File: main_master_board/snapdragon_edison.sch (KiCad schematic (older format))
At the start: 4 parts, among them U17 conn_2x45, U18 conn_2x45

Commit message: Added a lot of things. Put a 5v to 4v buck as well as supporing the snapdragon board
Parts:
- removed J?: USB_MICRO_RIGHT, MF_Connectors_MICROUSB-RIGHT, symbol USB_MICRO_RIGHT
- removed SD?: SD_CARD_SLOT_MICRO_RIGHT, MF_Connectors_MF-MICROSD, symbol SD_CARD_SLOT_MICRO_RIGHT
- added C33: 4.7uF, Capacitors_SMD:C_0603, symbol C_Small
- added C34, C35, C36, C37, C38, C39, C41, C42, C43, C44, C45, C46, C47, C48, C49, C50: 0.1uF, Capacitors_SMD:C_0402, symbol C_Small
- added C40: 1.0uF, Capacitors_SMD:C_0402, symbol C_Small
- added C53: 1.0uF, Capacitors_SMD:C_0603, symbol C_Small
- added C56, C57: 1uF, Capacitors_SMD:C_0603, symbol C_Small
- added J2: J0C-0005NLT, Pulse_Electronics:J0C, symbol RJ45
- added L4, L5: 2.0A/0.05 DCR, dp_devices2:dp_devices-C603, symbol Ferrite_Bead_Small
- added R24: 33, Resistors_SMD:R_0402, symbol R
- added R26: 825, Resistors_SMD:R_0603, symbol R
- added R27, R29: 10.0K, Resistors_SMD:R_0603, symbol R
- added R30: 12.4K, Resistors_SMD:R_0603, symbol R
- added R32: 12.0K, Resistors_SMD:R_0603, symbol R
- added R46, R47, R48, R50: 49.9, Resistors_SMD:R_0402, symbol R
- added R49: 10.0, Resistors_SMD:R_0402, symbol R
- added R56, R57, R58, R59: 33, Resistors_SMD:R_0402, symbol R_Small
- added R67, R68: 1K, Resistors_SMD:R_0402, symbol R
- added U19: LAN9512, Housings_DFN_QFN:QFN-64-1EP_9x9mm_Pitch0.5mm, symbol LAN9512
- added U21: MIC2026, SOIC_8:SOIC-8_N, symbol MIC2026
- added U24: AS1360, TO_SOT_Packages_SMD:SOT-23, symbol AS1360
- added U25: Si1900DL, NASA_IRG_SSB:SOT323-6, symbol Si1900DL
- added U26, U27: SN74LV4T125, VQFN-14:VQFN-14, symbol SN74LV4T125
- added U28: SN74LV1T125, TO_SOT_Packages_SMD:SC-70, symbol SN74LV1T125
- added Y1: SG-310SCCN 25.000MJ3, Seiko_Epson_Crystals:SG-310, symbol Crystal_GND24
- U17: value conn_2x45 -> J1; footprint Variscite:DART-SD410 -> MODULE
- U18: value conn_2x45 -> J2
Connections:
- net labels added: +1V8, +3.3VA, 1V8, APQ_RESIN_N, BBCLK2, BOOT_CONFIG_0, BOOT_CONFIG_1, BOOT_CONFIG_2, BOOT_CONFIG_3, BOOT_CONFIG_5, EEPROM_WP, FORCED_USB_BOOT, GPIO_105, GPIO_106, GPIO_107, GPIO_108, GPIO_109, GPIO_110, GPIO_112, GPIO_113, GPIO_114, GPIO_115, GPIO_116, GPIO_117, GPIO_118, GPIO_119, GPIO_12, GPIO_120, GPIO_13, GPIO_20, GPIO_21, GPIO_24, GPIO_25, GPIO_26, GPIO_27, GPIO_28, GPIO_29, GPIO_30, GPIO_31, GPIO_32, GPIO_33, GPIO_34, GPIO_35, GPIO_36, GPIO_49, GPIO_50, GPIO_51, GPIO_52, GPIO_62, GPIO_69, GPIO_96, GPIO_97, GPIO_98, I2C0_SCL, I2C0_SCL_3V3, I2C0_SDA, I2C0_SDA_3V3, I2C1_SCL, I2C1_SDA, I2C3_SCL, I2C3_SDA, JTAG_PS_HOLD, JTAG_SRST_N, JTAG_TCK, JTAG_TDI, JTAG_TDO, JTAG_TMS, JTAG_TRST_N, PM_GPIO1, PM_GPIO2, PM_GPIO3, PM_GPIO4, PM_MPP2, PM_MPP3, PM_MPP4, PM_RESIN_N, PRTCTL2, PRTCTL3, PWR2, PWR3, RXN, RXP, SDC2_CLK, SDC2_CMD, SDC2_DATA_0, SDC2_DATA_1, SDC2_DATA_2, SDC2_DATA_3, SD_CARD_DET_N, SPI0_CLK, SPI0_CS_N, SPI0_MISO, SPI0_MOSI, SPI1_CLK, SPI1_CLK_3V3, SPI1_CS_N, SPI1_CS_N_3V3, SPI1_MISO, SPI1_MISO_3V3, SPI1_MOSI, SPI1_MOSI_3V3, TXN, TXP, UART0_CTS_N, UART0_RTS_N, UART0_RX, UART0_TX, UART1_RX, UART1_RX_3V3, UART1_TX, UART1_TX_3V3, USBDM0, USBDM2, USBDP0, USBDP2, USBDP3, USBPM3, USB_HS_D_M, USB_HS_D_P, USB_HS_ID, USB_VBUS, VBUS_DET, VDD18ETHPLL, VDD18USBPLL, VREG_L11_SDC, VREG_L12_SDC, XI, nRESET, power_on/off, sensor_I2C_SCL, sensor_I2C_SDA, uC_CLK, uC_CS, uC_GPIO1, uC_GPIO2, uC_MISO, uC_MOSI, uC_reset
- net labels removed: I2C_SCL, I2C_SDA, prog_~UART_CTS, prog_~UART_RTS
- wire segments 0 -> 360
- no-connect marks 0 -> 66
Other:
- note added: "100 Ohm Differential Pairs"
- note added: "90 Ohm Differential Pairs"
- note added: "CT-RD"
- note added: "CT-TD"
- note added: "Down Converter\n3V3 -> 1V8"
- note added: "FM_ANTENNA"
- note added: "GND"
- note added: "Headphones"
- note added: "LAN9512 Power Filtering"
- note added: "MIPI CSI Camera"
- note added: "MIPI CSI \nCamera"
- note added: "MIPI DSI Camera"
- note added: "Mic"
- note added: "NC"
- note added: "OUT"
- note added: "RD+"
- note added: "RD-"
- note added: "Rs might not be needed"
- note added: "Speakers"
- note added: "TD+"
- note added: "TD-"
- note added: "Tantalum"
- note added: "Up Converter\n1V8 -> 3V3"
- note added: "VCC"
- note added: "place 1.0uF near lan9512"
- note added: "place 4.7uF near lan9512"
- note added: "place near lan9512"
- note added: "place near rj45"
- note added: "~ST"

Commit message: Cleaned up some wires and moved connectors out to main page. Also added some LEDs
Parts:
- removed R56, R57, R58, R59: 33, Resistors_SMD:R_0402, symbol R_Small
- U21: symbol MIC2026 -> MIC2026-RESCUE-main_master_board
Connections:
- wire segments 360 -> 356
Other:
- note added: "Trace impedence of 50-75 ohms"
- note removed: "Rs might not be needed"
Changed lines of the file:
@@
 LIBS:Sensors
 LIBS:LP3852-3.3
-LIBS:decaWave
+LIBS:0s102011ma1qn1
+LIBS:74LVC1G17
+LIBS:74V1T126
+LIBS:acs711klctr-12ab-t
+LIBS:AD7192
+LIBS:AD7193
+LIBS:am-hrr30-xxx
+LIBS:aon7528
+LIBS:AP7363
+LIBS:AS1359
+LIBS:csd16323q3
+LIBS:dmn2004dmk
+LIBS:dp_devices
+LIBS:DSPIC33E128MC506
+LIBS:fds6898az
+LIBS:ina197
+LIBS:irf7329pbf
+LIBS:ld1117
+LIBS:lm3478
+LIBS:lm3481
+LIBS:lt1910
+LIBS:ltc1871
+LIBS:ltc1982
+LIBS:MAG3110
+LIBS:mcp1700
+LIBS:mcp73831
+LIBS:mcsmt-g5030a1-3712
+LIBS:microchip_can
+LIBS:microclasp_hdrx2
+LIBS:microclasp_hdrx3
+LIBS:MPU-6000_MPU-6050
+LIBS:MPU-9150
+LIBS:nrf24l01+
+LIBS:pds1040l
+LIBS:pic12f1571
+LIBS:pinhead
+LIBS:psmn013-80ys
+LIBS:RESISTOR_ARRAY
+LIBS:rf803d
+LIBS:RGB_LED
+LIBS:Si1970DH
+LIBS:sn65hvd232
+LIBS:ssc54
+LIBS:sw_push_4
+LIBS:tc74
+LIBS:TPS2113A
+LIBS:tps54540
+LIBS:vs-mbrb1635pbf
+LIBS:xal5050-562meb
+LIBS:xal6030-182mec
 LIBS:conn_2x50
 LIBS:conn_open_q_x2
@@
 LIBS:ac-dc
 LIBS:actel
-LIBS:allegro
 LIBS:Altera
 LIBS:analog_devices
@@
 LIBS:logo
 LIBS:maxim
-LIBS:mechanical
 LIBS:microchip_dspic33dsc
 LIBS:microchip_pic10mcu
@@
 LIBS:microchip_pic32mcu
 LIBS:motor_drivers
-LIBS:motors
 LIBS:msp430
 LIBS:nordicsemi
@@
 LIBS:ttl_ieee
 LIBS:video
-LIBS:wiznet
 LIBS:Worldsemi
 LIBS:Xicor
-LIBS:zetex
 LIBS:Zilog
 LIBS:conn_2x45
@@
 $Descr A3 16535 11693
 encoding utf-8
-Sheet 6 7
+Sheet 5 6
 Title ""
 Date ""
@@
 GND
 $Comp
-L +3.3VA #PWR22
+L +3.3VA #PWR025
 U 1 1 58837660
 P 3025 5775
-F 0 "#PWR22" H 3025 5625 50  0001 C CNN
+F 0 "#PWR025" H 3025 5625 50  0001 C CNN
 F 1 "+3.3VA" H 3025 5915 50  0000 C CNN
 F 2 "" H 3025 5775 50  0000 C CNN
@@
 GND
 $Comp
-L +1V8 #PWR21
+L +1V8 #PWR026
 U 1 1 5884251A
 P 875 7125
-F 0 "#PWR21" H 875 6975 50  0001 C CNN
+F 0 "#PWR026" H 875 6975 50  0001 C CNN
 F 1 "+1V8" H 875 7265 50  0000 C CNN
 F 2 "" H 875 7125 50  0000 C CNN
@@
 3V3
 $Comp
-L +3.3VA #PWR24
+L +3.3VA #PWR027
 U 1 1 5884804C
 P 7725 5500
-F 0 "#PWR24" H 7725 5350 50  0001 C CNN
+F 0 "#PWR027" H 7725 5350 50  0001 C CNN
 F 1 "+3.3VA" H 7725 5640 50  0000 C CNN
 F 2 "" H 7725 5500 50  0000 C CNN
@@
 $EndComp
 $Comp
-L +1V8 #PWR23
+L +1V8 #PWR028
 U 1 1 58849901
 P 4400 6225
-F 0 "#PWR23" H 4400 6075 50  0001 C CNN
+F 0 "#PWR028" H 4400 6075 50  0001 C CNN
 F 1 "+1V8" H 4400 6365 50  0000 C CNN
 F 2 "" H 4400 6225 50  0000 C CNN
@@
 NoConn ~ 7575 8250
 $Comp
-L MIC2026 U21
+L MIC2026-RESCUE-main_master_board U21
 U 1 1 5885A971
 P 10725 6650
+AR Path="/5885A971" Ref="U21"  Part="1"
+AR Path="/587AA41C/5885A971" Ref="U21"  Part="1"
 F 0 "U21" H 10725 6350 50  0000 C CNN
 F 1 "MIC2026" H 10725 6950 50  0000 C CNN
@@
 $EndComp
 $Comp
-L +3.3VA #PWR25
+L +3.3VA #PWR029
 U 1 1 5885B0EB
 P 10325 8100
-F 0 "#PWR25" H 10325 7950 50  0001 C CNN
+F 0 "#PWR029" H 10325 7950 50  0001 C CNN
 F 1 "+3.3VA" H 10325 8240 50  0000 C CNN
 F 2 "" H 10325 8100 50  0000 C CNN
@@
 Wire Wire Line
 	8025 1125 8625 1125
-$Comp
-L R_Small R56
-U 1 1 58878C30
-P 14475 1450
-F 0 "R56" V 14525 1525 50  0000 L CNN
-F 1 "33" V 14475 1425 50  0000 L CNN
-F 2 "Resistors_SMD:R_0402" H 14475 1450 50  0001 C CNN
-F 3 "" H 14475 1450 50  0000 C CNN
-	1    14475 1450
-	0    1    1    0
-$EndComp
-$Comp
-L R_Small R57
-U 1 1 58878C37
-P 14475 1550
-F 0 "R57" V 14525 1625 50  0000 L CNN
-F 1 "33" V 14475 1525 50  0000 L CNN
-F 2 "Resistors_SMD:R_0402" H 14475 1550 50  0001 C CNN
-F 3 "" H 14475 1550 50  0000 C CNN
-	1    14475 1550
-	0    1    1    0
-$EndComp
-$Comp
-L R_Small R58
-U 1 1 58878C3E
-P 14475 1650
-F 0 "R58" V 14525 1725 50  0000 L CNN
-F 1 "33" V 14475 1625 50  0000 L CNN
-F 2 "Resistors_SMD:R_0402" H 14475 1650 50  0001 C CNN
-F 3 "" H 14475 1650 50  0000 C CNN
-	1    14475 1650
-	0    1    1    0
-$EndComp
-$Comp
-L R_Small R59
-U 1 1 58878C9D
-P 14475 1750
-F 0 "R59" V 14525 1825 50  0000 L CNN
-F 1 "33" V 14475 1725 50  0000 L CNN
-F 2 "Resistors_SMD:R_0402" H 14475 1750 50  0001 C CNN
-F 3 "" H 14475 1750 50  0000 C CNN
-	1    14475 1750
-	0    1    1    0
-$EndComp
-Wire Wire Line
-	14575 1450 14700 1450
-Wire Wire Line
-	14575 1550 14700 1550
-Wire Wire Line
-	14575 1650 14700 1650
-Wire Wire Line
-	14575 1750 14700 1750
-Text Notes 14425 1400 0    39   ~ 0
-Rs might not be needed
 Text HLabel 14700 900  2    60   BiDi ~ 0
 sensor_I2C_SDA
@@
 Wire Wire Line
 	14700 1000 14025 1000
-Text Label 14350 1450 2    60   ~ 0
+Text Label 14675 1450 2    60   ~ 0
 SPI1_MOSI_3V3
-Text Label 14350 1650 2    60   ~ 0
+Text Label 14675 1650 2    60   ~ 0
 SPI1_CS_N_3V3
-Text Label 14350 1750 2    60   ~ 0
+Text Label 14675 1750 2    60   ~ 0
 SPI1_CLK_3V3
 Text Label 14050 2050 0    60   ~ 0
 UART1_TX_3V3
 Wire Wire Line
-	14375 1450 13650 1450
-Wire Wire Line
-	14375 1650 13650 1650
-Wire Wire Line
-	14375 1750 13700 1750
+	14700 1450 13975 1450
+Wire Wire Line
+	14700 1650 13975 1650
+Wire Wire Line
+	14700 1750 14025 1750
 Wire Wire Line
 	14025 2050 14700 2050
@@
 Wire Wire Line
 	9825 1325 10500 1325
-Text Label 14350 1550 2    60   ~ 0
+Text Label 14675 1550 2    60   ~ 0
 SPI1_MISO_3V3
 Wire Wire Line
-	13675 1550 14375 1550
+	14000 1550 14700 1550
 Text Label 14675 1950 2    60   ~ 0
 UART1_RX_3V3
@@
 	9275 1925 9275 1975
 Connection ~ 9275 1975
+Text Notes 7550 900  0    39   ~ 0
+Trace impedence of 50-75 ohms
+Text Notes 13650 1325 0    39   ~ 0
+Trace impedence of 50-75 ohms
 $EndSCHEMATC

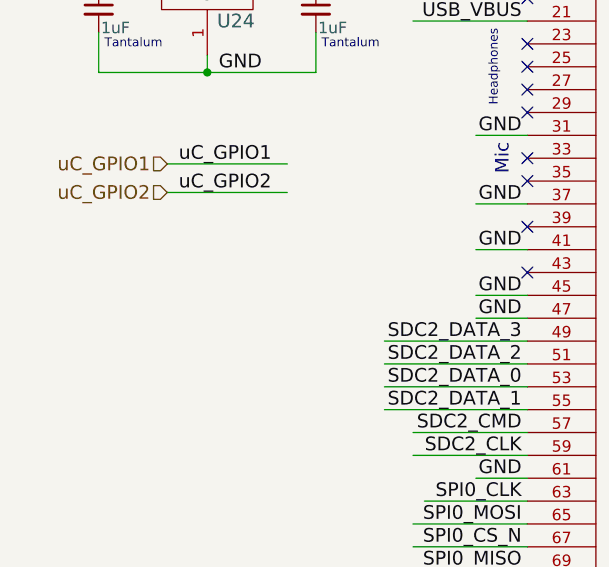
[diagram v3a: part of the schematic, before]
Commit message: Routed the 24-5 buck and added the dart board footprint
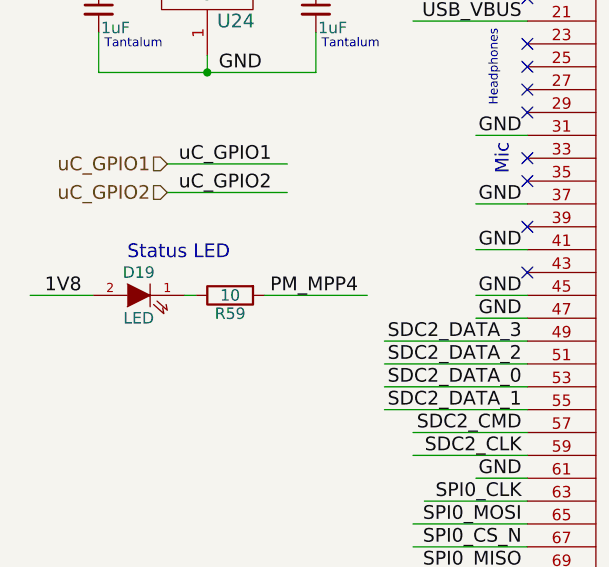
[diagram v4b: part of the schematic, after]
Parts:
- added D19: LED, LEDs:LED_0603, symbol LED
- added R59: 10, Resistors_SMD:R_0603, symbol R
- U17: footprint MODULE -> Variscite:DART-SD410
- U18: footprint MODULE -> Hirose:DF40HC(3.0)-90DS-0.4V(51)
- U28: footprint TO_SOT_Packages_SMD:SC-70 -> SO-70:SO-70
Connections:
- wire segments 356 -> 359
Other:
- note added: "Status LED"
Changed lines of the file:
@@
 LIBS:Sensors
 LIBS:LP3852-3.3
-LIBS:decaWave
+LIBS:0s102011ma1qn1
+LIBS:74LVC1G17
+LIBS:74V1T126
+LIBS:acs711klctr-12ab-t
+LIBS:AD7192
+LIBS:AD7193
+LIBS:am-hrr30-xxx
+LIBS:aon7528
+LIBS:AP7363
+LIBS:AS1359
+LIBS:csd16323q3
+LIBS:dmn2004dmk
+LIBS:dp_devices
+LIBS:DSPIC33E128MC506
+LIBS:fds6898az
+LIBS:ina197
+LIBS:irf7329pbf
+LIBS:ld1117
+LIBS:lm3478
+LIBS:lm3481
+LIBS:lt1910
+LIBS:ltc1871
+LIBS:ltc1982
+LIBS:MAG3110
+LIBS:mcp1700
+LIBS:mcp73831
+LIBS:mcsmt-g5030a1-3712
+LIBS:microchip_can
+LIBS:microclasp_hdrx2
+LIBS:microclasp_hdrx3
+LIBS:MPU-6000_MPU-6050
+LIBS:MPU-9150
+LIBS:nrf24l01+
+LIBS:pds1040l
+LIBS:pic12f1571
+LIBS:pinhead
+LIBS:psmn013-80ys
+LIBS:RESISTOR_ARRAY
+LIBS:rf803d
+LIBS:RGB_LED
+LIBS:Si1970DH
+LIBS:sn65hvd232
+LIBS:ssc54
+LIBS:sw_push_4
+LIBS:tc74
+LIBS:TPS2113A
+LIBS:tps54540
+LIBS:vs-mbrb1635pbf
+LIBS:xal5050-562meb
+LIBS:xal6030-182mec
 LIBS:conn_2x50
 LIBS:conn_open_q_x2
@@
 LIBS:ac-dc
 LIBS:actel
-LIBS:allegro
 LIBS:Altera
 LIBS:analog_devices
@@
 LIBS:logo
 LIBS:maxim
-LIBS:mechanical
 LIBS:microchip_dspic33dsc
 LIBS:microchip_pic10mcu
@@
 LIBS:microchip_pic32mcu
 LIBS:motor_drivers
-LIBS:motors
 LIBS:msp430
 LIBS:nordicsemi
@@
 LIBS:ttl_ieee
 LIBS:video
-LIBS:wiznet
 LIBS:Worldsemi
 LIBS:Xicor
-LIBS:zetex
 LIBS:Zilog
 LIBS:conn_2x45
@@
 F 0 "U17" H 3250 2900 50  0000 C CNN
 F 1 "J1" H 3250 3100 50  0000 C CNN
-F 2 "MODULE" H 3250 3000 50  0001 C CNN
+F 2 "Variscite:DART-SD410" H 3250 3000 50  0001 C CNN
 F 3 "DOCUMENTATION" H 3250 3000 50  0001 C CNN
 	1    3250 3000
@@
 F 0 "U18" H 5700 2900 50  0000 C CNN
 F 1 "J2" H 5700 3100 50  0000 C CNN
-F 2 "MODULE" H 5700 3000 50  0001 C CNN
+F 2 "Hirose:DF40HC(3.0)-90DS-0.4V(51)" H 5700 3000 50  0001 C CNN
 F 3 "DOCUMENTATION" H 5700 3000 50  0001 C CNN
 	1    5700 3000
@@
 F 0 "U28" H 11650 925 50  0000 C CNN
 F 1 "SN74LV1T125" H 11650 1425 50  0000 C CNN
-F 2 "TO_SOT_Packages_SMD:SC-70" H 11650 1175 50  0001 C CNN
+F 2 "SO-70:SO-70" H 11650 1175 50  0001 C CNN
 F 3 "http://www.ti.com/lit/ds/symlink/sn74lv1t125.pdf" H 11650 1175 50  0001 C CNN
 	1    11650 1175
@@
 Text Notes 13650 1325 0    39   ~ 0
 Trace impedence of 50-75 ohms
+$Comp
+L LED D19
+U 1 1 5889689C
+P 1050 3000
+F 0 "D19" H 1050 3100 50  0000 C CNN
+F 1 "LED" H 1050 2900 50  0000 C CNN
+F 2 "LEDs:LED_0603" H 1050 3000 50  0001 C CNN
+F 3 "http://www.digikey.com/product-detail/en/lumex-opto-components-inc/SML-LX0603SRW-TR/67-1551-1-ND/304364" H 1050 3000 50  0001 C CNN
+	1    1050 3000
+	-1   0    0    -1
+$EndComp
+$Comp
+L R R59
+U 1 1 588974DF
+P 1450 3000
+F 0 "R59" V 1530 3000 50  0000 C CNN
+F 1 "10" V 1450 3000 50  0000 C CNN
+F 2 "Resistors_SMD:R_0603" V 1380 3000 50  0001 C CNN
+F 3 "" H 1450 3000 50  0001 C CNN
+	1    1450 3000
+	0    -1   1    0
+$EndComp
+Wire Wire Line
+	1250 3000 1300 3000
+Wire Wire Line
+	850  3000 575  3000
+Text Label 800  3000 2    60   ~ 0
+1V8
+Wire Wire Line
+	1600 3000 2050 3000
+Text Label 1625 3000 0    60   ~ 0
+PM_MPP4
+Text Notes 1000 2850 0    60   ~ 0
+Status LED
 $EndSCHEMATC

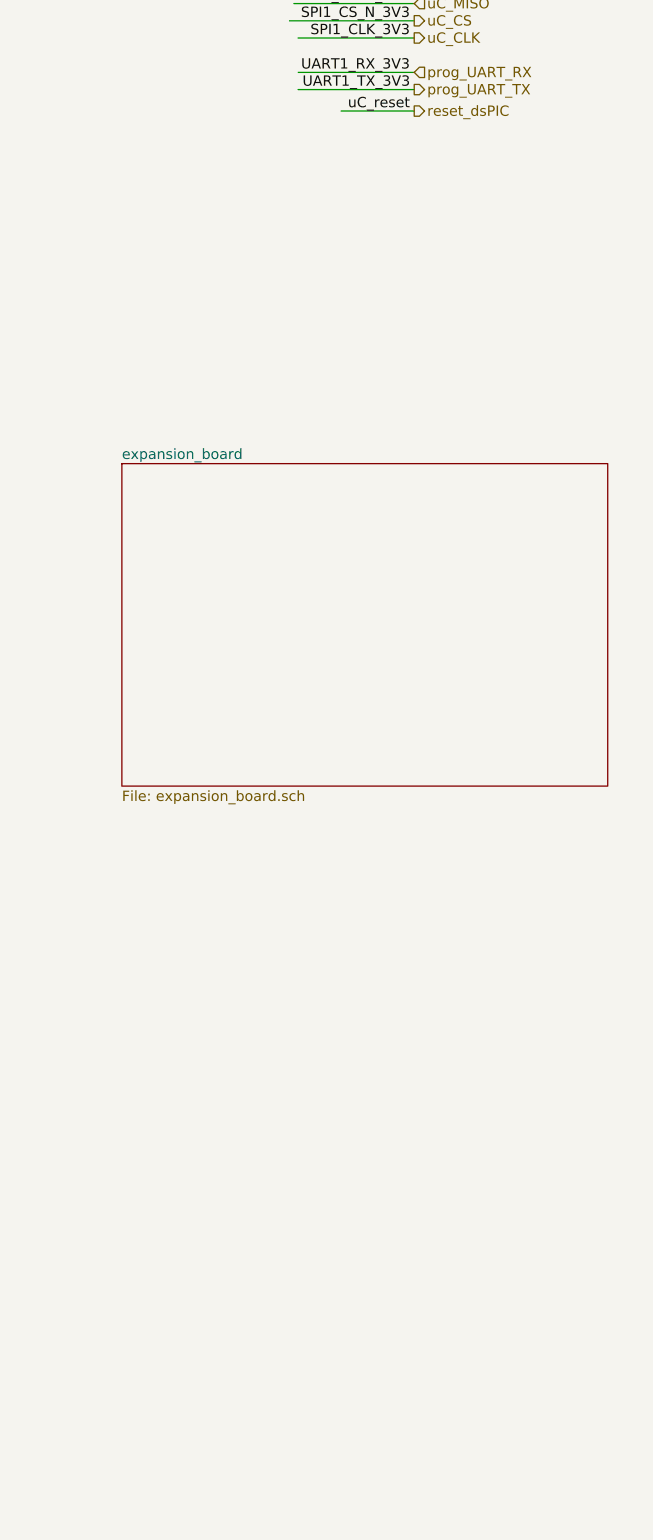
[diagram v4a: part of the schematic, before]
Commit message: Routing power. Added 5V leveling cap.
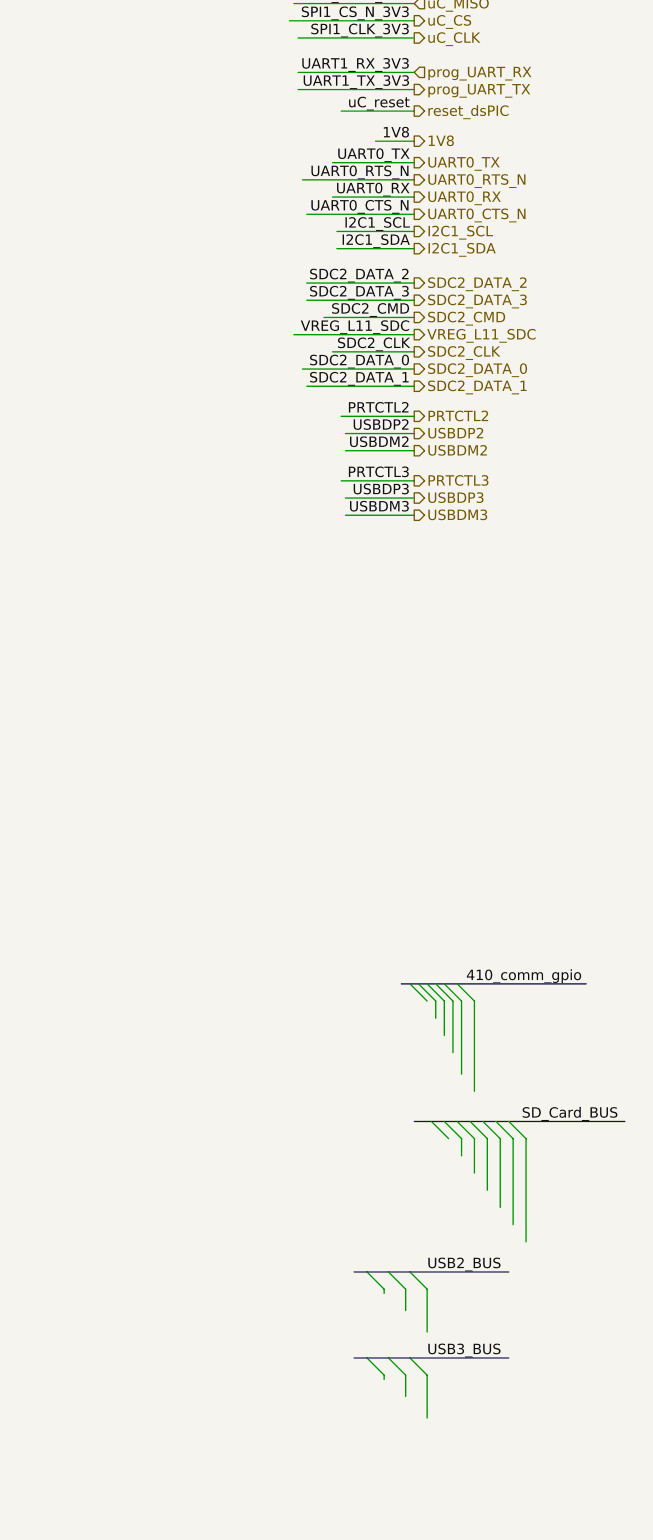
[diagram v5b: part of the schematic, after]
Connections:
- net labels added: 410_comm_gpio, SD_Card_BUS, USB2_BUS, USB3_BUS, USBDM3
- wire segments 359 -> 396

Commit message: Added stuff and routing
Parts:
- D19: symbol LED -> LED-RESCUE-main_master_board
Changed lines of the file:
@@
 LIBS:Sensors
 LIBS:LP3852-3.3
-LIBS:0s102011ma1qn1
-LIBS:74LVC1G17
-LIBS:74V1T126
-LIBS:acs711klctr-12ab-t
-LIBS:AD7192
-LIBS:AD7193
-LIBS:am-hrr30-xxx
-LIBS:aon7528
-LIBS:AP7363
-LIBS:AS1359
-LIBS:csd16323q3
-LIBS:dmn2004dmk
-LIBS:dp_devices
-LIBS:DSPIC33E128MC506
-LIBS:fds6898az
-LIBS:ina197
-LIBS:irf7329pbf
-LIBS:ld1117
-LIBS:lm3478
-LIBS:lm3481
-LIBS:lt1910
-LIBS:ltc1871
-LIBS:ltc1982
-LIBS:MAG3110
-LIBS:mcp1700
-LIBS:mcp73831
-LIBS:mcsmt-g5030a1-3712
-LIBS:microchip_can
-LIBS:microclasp_hdrx2
-LIBS:microclasp_hdrx3
-LIBS:MPU-6000_MPU-6050
-LIBS:MPU-9150
-LIBS:nrf24l01+
-LIBS:pds1040l
-LIBS:pic12f1571
-LIBS:pinhead
-LIBS:psmn013-80ys
-LIBS:RESISTOR_ARRAY
-LIBS:rf803d
-LIBS:RGB_LED
-LIBS:Si1970DH
-LIBS:sn65hvd232
-LIBS:ssc54
-LIBS:sw_push_4
-LIBS:tc74
-LIBS:TPS2113A
-LIBS:tps54540
-LIBS:vs-mbrb1635pbf
-LIBS:xal5050-562meb
-LIBS:xal6030-182mec
+LIBS:decaWave
 LIBS:conn_2x50
 LIBS:conn_open_q_x2
@@
 LIBS:ac-dc
 LIBS:actel
+LIBS:allegro
 LIBS:Altera
 LIBS:analog_devices
@@
 LIBS:logo
 LIBS:maxim
+LIBS:mechanical
 LIBS:microchip_dspic33dsc
 LIBS:microchip_pic10mcu
@@
 LIBS:microchip_pic32mcu
 LIBS:motor_drivers
+LIBS:motors
 LIBS:msp430
 LIBS:nordicsemi
@@
 LIBS:ttl_ieee
 LIBS:video
+LIBS:wiznet
 LIBS:Worldsemi
 LIBS:Xicor
+LIBS:zetex
 LIBS:Zilog
 LIBS:conn_2x45
@@
 Trace impedence of 50-75 ohms
 $Comp
-L LED D19
+L LED-RESCUE-main_master_board D19
 U 1 1 5889689C
 P 1050 3000
+AR Path="/5889689C" Ref="D19"  Part="1"
+AR Path="/587AA41C/5889689C" Ref="D19"  Part="1"
 F 0 "D19" H 1050 3100 50  0000 C CNN
 F 1 "LED" H 1050 2900 50  0000 C CNN
